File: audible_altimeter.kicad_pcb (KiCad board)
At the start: 2 copper layers, 0 parts

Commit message: Start adding power components
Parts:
- added CON1: BUQ2-USB-MICRO-B, buq2:USB-MICRO-B-FCI, F.Cu at (75.0, 15.5)
- added IC1: BUQ2-ATXMEGA128A4U-A, buq2:BUQ2-TQFP44, F.Cu at (59.5, 69.5)
- added LS013B4DN04-FPC: VAL**, buq2:LS013B4DN04-FPC, F.Cu at (70.0, 55.0)
- added MOUNTING_HOLE: VAL**, buq2:MOUNTING_HOLE, F.Cu at (52.0, 26.0)
- added MOUNTING_HOLE: VAL**, buq2:MOUNTING_HOLE, F.Cu at (95.0, 26.0)
- added MOUNTING_HOLE: VAL**, buq2:MOUNTING_HOLE, F.Cu at (52.0, 54.0)
- added MOUNTING_HOLE: VAL**, buq2:MOUNTING_HOLE, F.Cu at (95.0, 54.0)
- added U1: MPL3115A2, buq2:8-TLGA, F.Cu at (114.5, 63.0)
- added U2: TAG-CONNECT-ATMEL-PDI-CONNECTOR, buq2:TAG-CONNECT6, F.Cu at (118.5, 50.5)
- added U3: MICRO-SD-CONN, buq2:MICRO-SD-CONN-AMPHENOL-PUSH-PUSH, F.Cu at (62.0, 2.00)
- added U4: MPU-9250, buq2:24QFN-3MM-3MM, F.Cu at (109.0, 73.5)
- added U5: MCP7940M, buq2:8-TDFN, F.Cu at (104.5, 66.5)
- added U6: MCP73831-SOT-23-5, buq2:SOT-23-5, F.Cu at (83.5, 70.0)
- added U7: NCP4681-SC-70, buq2:SOT-353, F.Cu at (74.5, 62.0)
- added U8: CSS-0575A-SMT, buq2:BUZZER-CUI-5MM, F.Cu at (86.5, 28.0)
- added U9: LS013B4DN04, buq2:FPC-CONN-10-FCI, F.Cu at (101.5, 12.0)

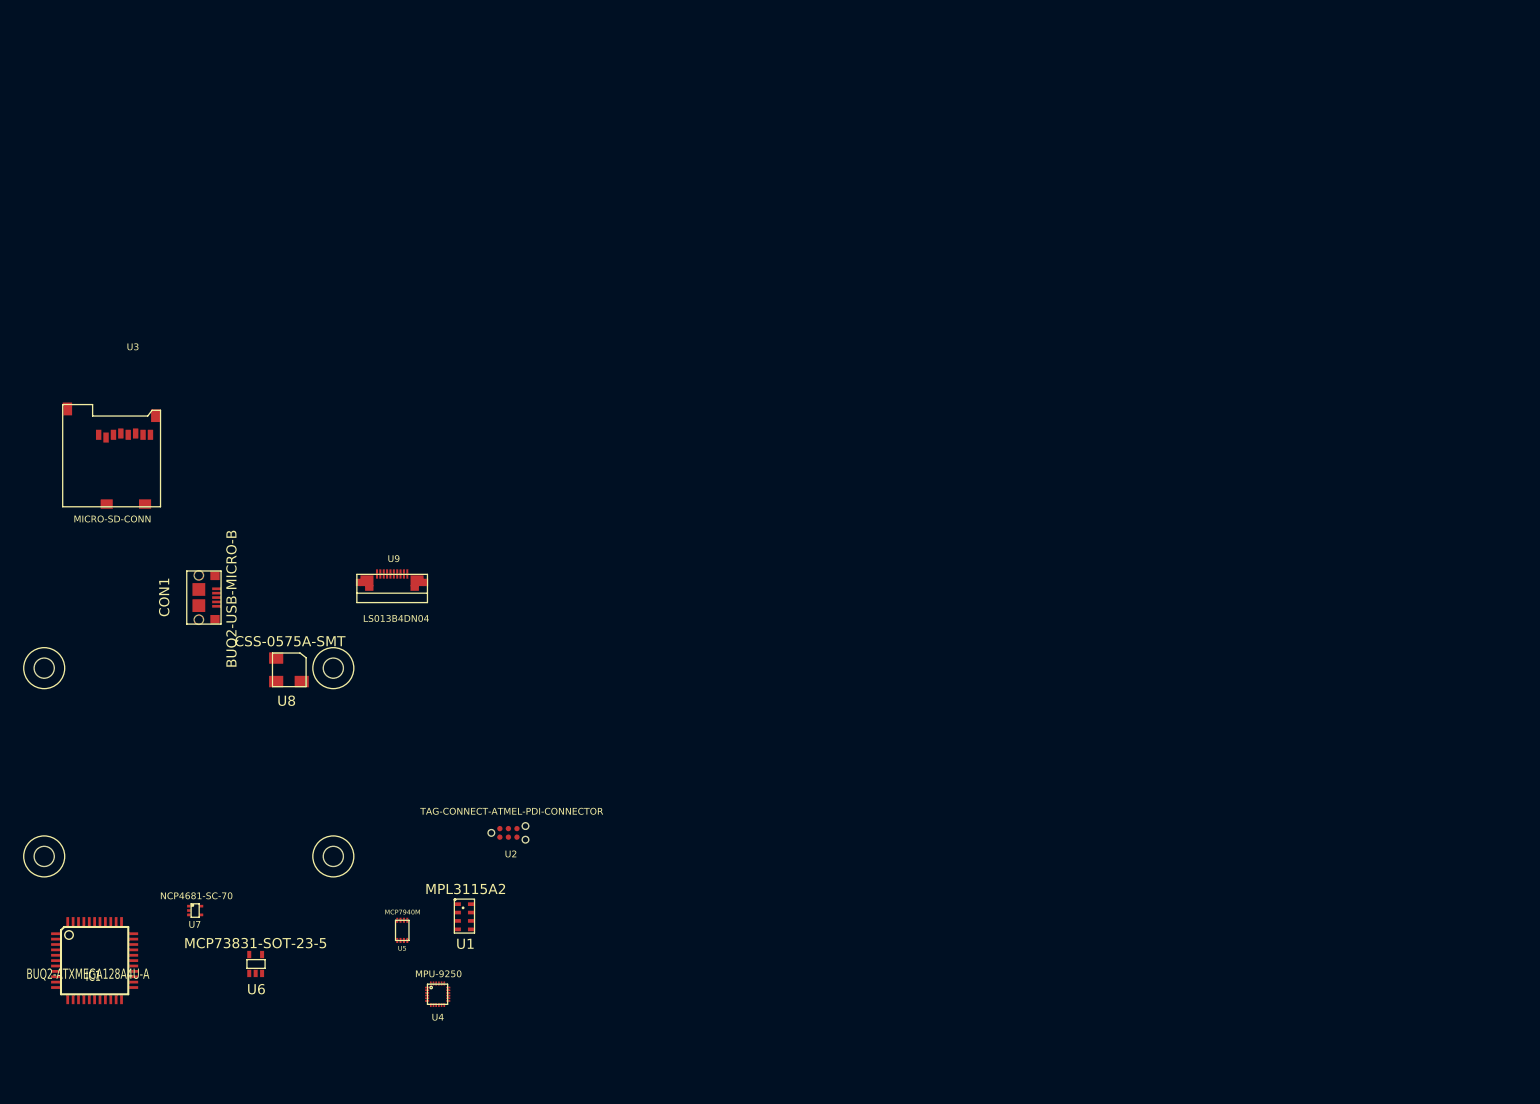
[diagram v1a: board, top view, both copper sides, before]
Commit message: Add gps
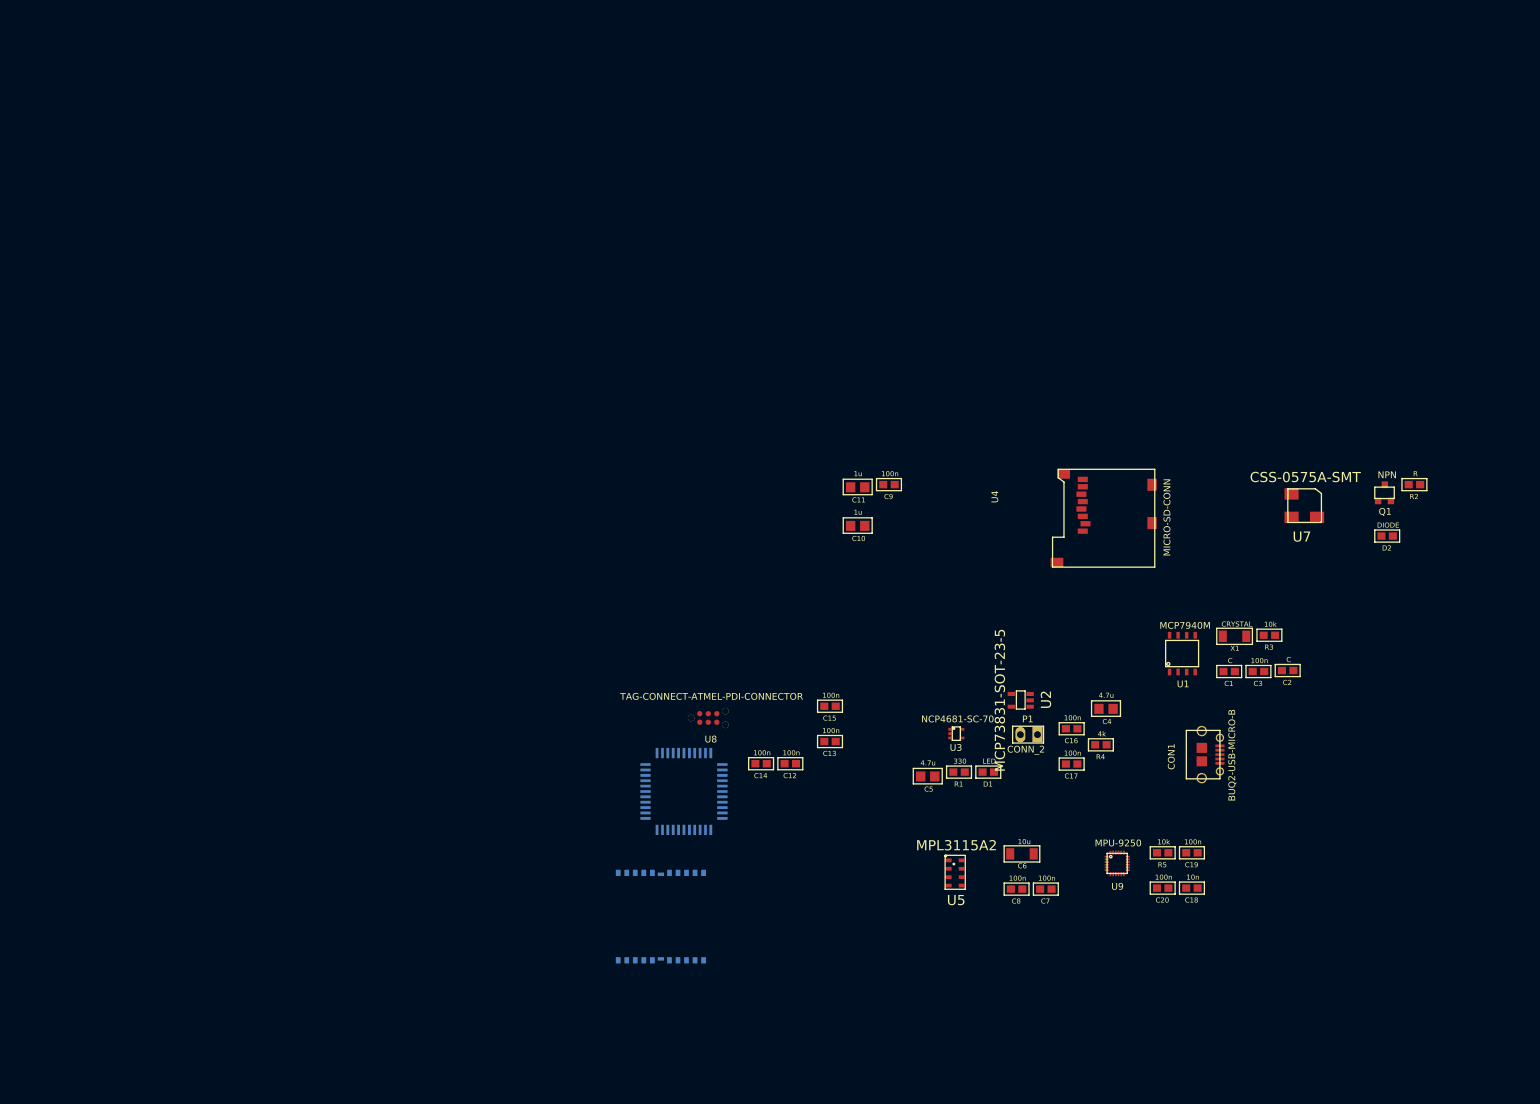
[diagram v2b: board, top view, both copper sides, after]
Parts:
- removed LS013B4DN04-FPC: VAL**, buq2:LS013B4DN04-FPC
- removed MOUNTING_HOLE (x4): VAL**, buq2:MOUNTING_HOLE
- added C1: C, buq2:SM0603, F.Cu at (228.2, 26.5)
- added C10: 1u, buq2:SM0805, F.Cu at (173.0, 4.84)
- added C11: 1u, buq2:SM0805, F.Cu at (173.0, -0.90)
- added C12: 100n, buq2:SM0603, F.Cu at (163.0, 40.2)
- added C13: 100n, buq2:SM0603, F.Cu at (168.9, 36.9)
- added C14: 100n, buq2:SM0603, F.Cu at (158.6, 40.2)
- added C15: 100n, buq2:SM0603, F.Cu at (168.9, 31.7)
- added C16: 100n, buq2:SM0603, F.Cu at (204.8, 35.0)
- added C17: 100n, buq2:SM0603, F.Cu at (204.8, 40.3)
- added C18: 10n, buq2:SM0603, F.Cu at (222.7, 58.7)
- added C19: 100n, buq2:SM0603, F.Cu at (222.7, 53.5)
- added C2: C, buq2:SM0603, F.Cu at (236.9, 26.4)
- added C20: 100n, buq2:SM0603, F.Cu at (218.3, 58.7)
- added C3: 100n, buq2:SM0603, F.Cu at (232.6, 26.5)
- added C4: 4.7u, buq2:SM0805, F.Cu at (209.9, 32.1)
- added C5: 4.7u, buq2:SM0805, F.Cu at (183.4, 42.1)
- added C6: 10u, buq2:SM1206, F.Cu at (197.4, 53.6)
- added C7: 100n, buq2:SM0603, F.Cu at (201.0, 58.9)
- added C8: 100n, buq2:SM0603, F.Cu at (196.6, 58.9)
- added C9: 100n, buq2:SM0603, F.Cu at (177.6, -1.30)
- added D1: LED, buq2:SM0603, F.Cu at (192.4, 41.5)
- added D2: DIODE, buq2:SM0603, F.Cu at (251.7, 6.35)
- added P1: CONN_2, buq2:PIN_HEADER_2, F.Cu at (202.1, 35.9)
- added Q1: NPN, buq2:SOT-23-3, F.Cu at (251.4, -0.07)
- added R1: 330, buq2:SM0603, F.Cu at (188.1, 41.5)
- added R2: R, buq2:SM0603, F.Cu at (255.8, -1.30)
- added R3: 10k, buq2:SM0603, F.Cu at (234.2, 21.1)
- added R4: 4k, buq2:SM0603, F.Cu at (209.2, 37.4)
- added R5: 10k, buq2:SM0603, F.Cu at (218.3, 53.5)
- added U10: LINX-FM-GPS, buq2:LINX-FM-GPS, B.Cu at (143.7, 63.0)
- added X1: CRYSTAL, buq2:SM1206, F.Cu at (229.0, 21.3)
- CON1: footprint buq2:USB-MICRO-B-FCI -> buq2:USB-MICRO-B-FCI-10118194
- IC1: moved to B.Cu
- U1: value MPL3115A2 -> MCP7940M; footprint buq2:8-TLGA -> buq2:8-SOIC
- U2: value TAG-CONNECT-ATMEL-PDI-CONNECTOR -> MCP73831-SOT-23-5; footprint buq2:TAG-CONNECT6 -> buq2:SOT-23-5
- U3: value MICRO-SD-CONN -> NCP4681-SC-70; footprint buq2:MICRO-SD-CONN-AMPHENOL-PUSH-PUSH -> buq2:SOT-353
- U4: value MPU-9250 -> MICRO-SD-CONN; footprint buq2:24QFN-3MM-3MM -> buq2:MICRO-SD-CONN-AMPHENOL-PUSH-PUSH
- U5: value MCP7940M -> MPL3115A2; footprint buq2:8-TDFN -> buq2:8-TLGA
- U6: value MCP73831-SOT-23-5 -> LS013B4DN04; footprint buq2:SOT-23-5 -> buq2:LS013B7DH03-FPC
- U7: value NCP4681-SC-70 -> CSS-0575A-SMT; footprint buq2:SOT-353 -> buq2:BUZZER-CUI-5MM
- U8: value CSS-0575A-SMT -> TAG-CONNECT-ATMEL-PDI-CONNECTOR; footprint buq2:BUZZER-CUI-5MM -> buq2:TAG-CONNECT6
- U9: value LS013B4DN04 -> MPU-9250; footprint buq2:FPC-CONN-10-FCI -> buq2:24QFN-3MM-3MM
- moved U7 173.2 mm to (237.5, 3.58)
- moved CON1 153.6 mm to (226.9, 38.9)
- moved U3 130.1 mm to (187.7, 35.7)
- moved U4 128.7 mm to (217.2, 3.73), turned to 90 degrees
- moved U9 116.4 mm to (210.1, 54.0)
- moved U1 111.0 mm to (219.4, 26.6)
- moved U6 103.9 mm to (168.1, 9.73), turned to 90 degrees
- moved IC1 91.2 mm to (147.1, 44.3)
- moved U5 83.6 mm to (187.5, 56.5)
- moved U2 81.2 mm to (197.2, 30.7), turned to 90 degrees
- moved U8 62.0 mm to (148.2, 33.4)
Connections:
- CON1 pad 1: Net-(CON1-Pad1) -> (no net)
- CON1 pad 2: Net-(CON1-Pad2) -> (no net)
- CON1 pad 3: Net-(CON1-Pad3) -> (no net)
- CON1 pad 4: Net-(CON1-Pad4) -> (no net)
- CON1 pad 5: Net-(CON1-Pad5) -> GND
- CON1 pad 6: Net-(CON1-Pad6) -> GND
- IC1 pad 1: Net-(IC1-Pad1) -> (no net)
- IC1 pad 10: Net-(IC1-Pad10) -> (no net)
- IC1 pad 11: Net-(IC1-Pad11) -> (no net)
- IC1 pad 12: Net-(IC1-Pad12) -> (no net)
- IC1 pad 13: Net-(IC1-Pad13) -> (no net)
- IC1 pad 14: Net-(IC1-Pad14) -> (no net)
- IC1 pad 15: Net-(IC1-Pad15) -> (no net)
- IC1 pad 16: Net-(IC1-Pad16) -> (no net)
- IC1 pad 17: Net-(IC1-Pad17) -> (no net)
- IC1 pad 18: Net-(IC1-Pad18) -> GND
- IC1 pad 19: Net-(IC1-Pad19) -> MCU_VCC
- IC1 pad 2: Net-(IC1-Pad2) -> (no net)
- IC1 pad 20: Net-(IC1-Pad20) -> (no net)
- IC1 pad 21: Net-(IC1-Pad21) -> (no net)
- IC1 pad 22: Net-(IC1-Pad22) -> (no net)
- IC1 pad 23: Net-(IC1-Pad23) -> (no net)
- IC1 pad 24: Net-(IC1-Pad24) -> (no net)
- IC1 pad 25: Net-(IC1-Pad25) -> (no net)
- IC1 pad 26: Net-(IC1-Pad26) -> (no net)
- IC1 pad 27: Net-(IC1-Pad27) -> (no net)
- IC1 pad 28: Net-(IC1-Pad28) -> (no net)
- IC1 pad 29: Net-(IC1-Pad29) -> (no net)
- IC1 pad 3: Net-(IC1-Pad3) -> (no net)
- IC1 pad 30: Net-(IC1-Pad30) -> GND
- IC1 pad 31: Net-(IC1-Pad31) -> MCU_VCC
- IC1 pad 32: Net-(IC1-Pad32) -> (no net)
- IC1 pad 33: Net-(IC1-Pad33) -> (no net)
- IC1 pad 34: Net-(IC1-Pad34) -> PDI_DATA
- IC1 pad 35: Net-(IC1-Pad35) -> PDI_CLK
- IC1 pad 36: Net-(IC1-Pad36) -> (no net)
- IC1 pad 37: Net-(IC1-Pad37) -> (no net)
- IC1 pad 38: Net-(IC1-Pad38) -> GND
- IC1 pad 39: Net-(IC1-Pad39) -> MCU_VCC
- IC1 pad 4: Net-(IC1-Pad4) -> (no net)
- IC1 pad 40: Net-(IC1-Pad40) -> (no net)
- IC1 pad 41: Net-(IC1-Pad41) -> (no net)
- IC1 pad 42: Net-(IC1-Pad42) -> (no net)
- IC1 pad 43: Net-(IC1-Pad43) -> (no net)
- IC1 pad 44: Net-(IC1-Pad44) -> (no net)
- IC1 pad 5: Net-(IC1-Pad5) -> (no net)
- IC1 pad 6: Net-(IC1-Pad6) -> (no net)
- IC1 pad 7: Net-(IC1-Pad7) -> (no net)
- IC1 pad 8: Net-(IC1-Pad8) -> GND
- IC1 pad 9: Net-(IC1-Pad9) -> MCU_VCC
- U1 pad 3: Net-(U1-Pad3) -> (no net)
- U1 pad 4: Net-(U1-Pad4) -> GND
- U1 pad 5: Net-(U1-Pad5) -> (no net)
- U1 pad 6: Net-(U1-Pad6) -> (no net)
- U1 pad 7: Net-(U1-Pad7) -> /Clock/MULTI_FUNCTIONAL
- U1 pad 8: Net-(U1-Pad8) -> /Clock/VCC
- U2 pad 2: Net-(U2-Pad2) -> GND
- U2 pad 3: Net-(U2-Pad3) -> /Battery/BATTERY
- U2 pad 4: Net-(U2-Pad4) -> /Battery/+5V
- U3 pad 1: Net-(U3-Pad1) -> /Battery/+5V
- U3 pad 2: Net-(U3-Pad2) -> (no net)
- U3 pad 3: Net-(U3-Pad3) -> GND
- U3 pad 4: Net-(U3-Pad4) -> /Battery/+3.3V
- U3 pad 5: Net-(U3-Pad5) -> /Battery/+5V
- U4 pad 1: Net-(U4-Pad1) -> (no net)
- U4 pad 10: Net-(U4-Pad10) -> GND
- U4 pad 2: Net-(U4-Pad2) -> (no net)
- U4 pad 3: Net-(U4-Pad3) -> (no net)
- U4 pad 4: Net-(U4-Pad4) -> (no net)
- U4 pad 5: Net-(U4-Pad5) -> (no net)
- U4 pad 6: Net-(U4-Pad6) -> GND
- U4 pad 7: Net-(U4-Pad7) -> (no net)
- U4 pad 8: Net-(U4-Pad8) -> (no net)
- U4 pad 9: Net-(U4-Pad9) -> (no net)
- U5 pad 1: Net-(U5-Pad1) -> /Barometer/VCC
- U5 pad 3: Net-(U5-Pad3) -> GND
- U5 pad 4: Net-(U5-Pad4) -> /Barometer/VCC
- U5 pad 5: Net-(U5-Pad5) -> (no net)
- U5 pad 6: Net-(U5-Pad6) -> (no net)
- U5 pad 7: Net-(U5-Pad7) -> (no net)
- U5 pad 8: Net-(U5-Pad8) -> (no net)
- U7 pad 1: Net-(U7-Pad1) -> /Buzzer/BATTERY
- U7 pad 3: Net-(U7-Pad3) -> (no net)
- U8 pad 1: Net-(U8-Pad1) -> PDI_DATA
- U8 pad 2: Net-(U8-Pad2) -> MCU_VCC
- U9 pad 1: Net-(U9-Pad1) -> /9-Axis/VDD
- U9 pad 2: Net-(U9-Pad2) -> (no net)
- U9 pad 3: Net-(U9-Pad3) -> (no net)
- U9 pad 4: Net-(U9-Pad4) -> (no net)
- U9 pad 5: Net-(U9-Pad5) -> (no net)
- U9 pad 6: Net-(U9-Pad6) -> (no net)
- U9 pad 7: Net-(U9-Pad7) -> (no net)
- U9 pad 8: Net-(U9-Pad8) -> /9-Axis/VDD
- U9 pad 9: Net-(U9-Pad9) -> GND

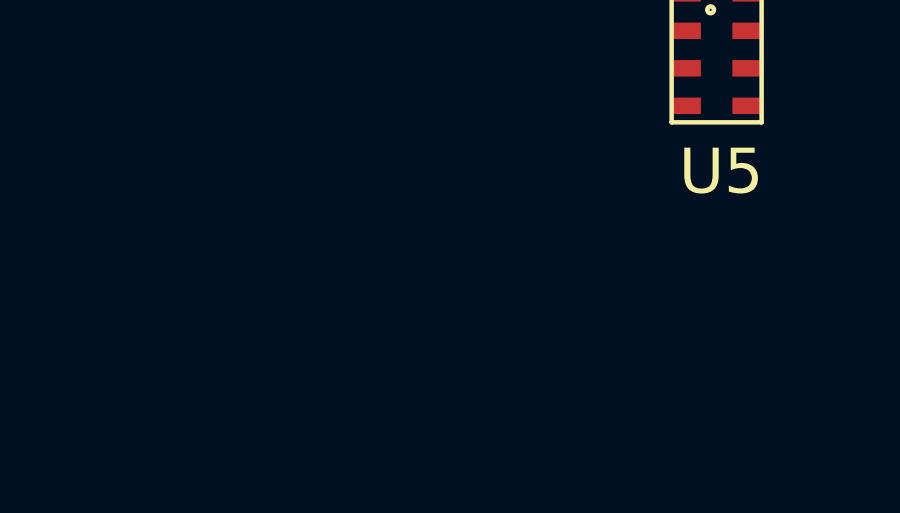
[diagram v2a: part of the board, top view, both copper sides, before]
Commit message: Add humidity sensor
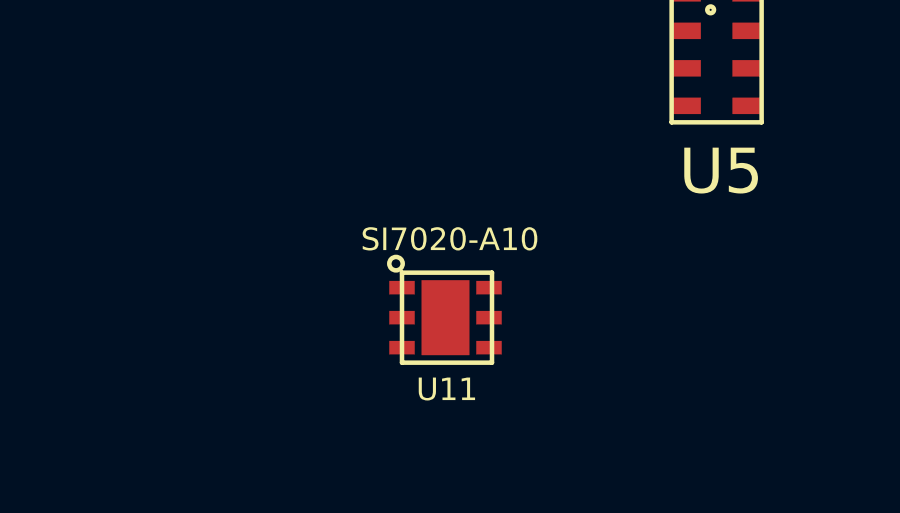
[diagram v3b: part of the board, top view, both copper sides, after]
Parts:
- added U11: SI7020-A10, buq2:DFN-6-3X3MM, F.Cu at (178.4, 65.4)
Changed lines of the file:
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@@
 (kicad_pcb (version 4) (host pcbnew "(2014-11-09 BZR 5259)-product")
   (general
-    (links 95)
-    (no_connects 95)
+    (links 96)
+    (no_connects 96)
     (area 0 0 0 0)
     (thickness 1.6)
@@
     (tracks 0)
     (zones 0)
-    (modules 42)
+    (modules 43)
     (nets 25)
   )
@@
       (net 3 "Net-(C2-Pad1)"))
   )
+  (module buq2:DFN-6-3X3MM (layer F.Cu)
+    (at 178.4 65.4)
+    (fp_text reference U11 (at 0.1 2.4) (layer F.SilkS)
+      (effects (font (size 0.75 0.75) (thickness 0.15)))
+    )
+    (fp_text value SI7020-A10 (at 0.2 -2.6) (layer F.SilkS)
+      (effects (font (size 0.75 0.75) (thickness 0.15)))
+    )
+    (fp_circle (center -1.6 -1.8) (end -1.5 -1.6) (layer F.SilkS) (width 0.15))
+    (fp_line (start -1.4 -1.5) (end 1.6 -1.5) (layer F.SilkS) (width 0.15))
+    (fp_line (start 1.6 1.5) (end -1.4 1.5) (layer F.SilkS) (width 0.15))
+    (fp_line (start -1.4 -1.5) (end -1.4 1.5) (layer F.SilkS) (width 0.15))
+    (fp_line (start 1.6 1.5) (end 1.6 -1.5) (layer F.SilkS) (width 0.15))
+    (pad 1 smd rect (at -1.4 -1) (size 0.85 0.45) (layers F.Cu F.Paste F.Mask))
+    (pad 2 smd rect (at -1.4 0) (size 0.85 0.45) (layers F.Cu F.Paste F.Mask)
+      (net 2 GND))
+    (pad 3 smd rect (at -1.4 1) (size 0.85 0.45) (layers F.Cu F.Paste F.Mask))
+    (pad 4 smd rect (at 1.5 1) (size 0.85 0.45) (layers F.Cu F.Paste F.Mask))
+    (pad 5 smd rect (at 1.5 0) (size 0.85 0.45) (layers F.Cu F.Paste F.Mask))
+    (pad 6 smd rect (at 1.5 -1) (size 0.85 0.45) (layers F.Cu F.Paste F.Mask))
+    (pad 7 smd rect (at 0.05 0) (size 1.6 2.5) (layers F.Cu F.Paste F.Mask))
+  )
   (gr_line (start 152 22.4) (end 99.6 22.4) (angle 90) (layer F.Fab) (width 0.2))
